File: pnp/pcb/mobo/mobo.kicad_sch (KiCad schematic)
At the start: 0 parts

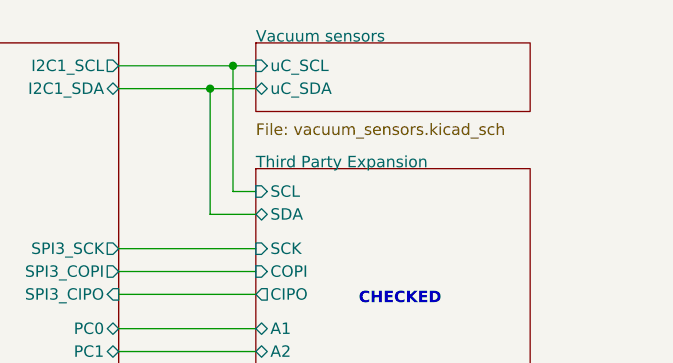
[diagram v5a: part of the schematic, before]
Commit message: Updated symbols and changed I2C multiplexer to a simpler one
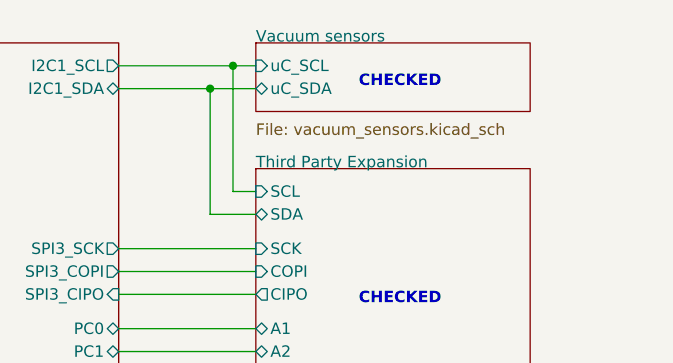
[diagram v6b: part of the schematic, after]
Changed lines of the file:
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@@
+    (effects (font (size 1.27 1.27) (thickness 0.254) bold (color 0 127 0 1)) (justify left bottom))
+  )
+  (text "CHECKED" (at 198.12 34.29 0)
     (effects (font (size 1.27 1.27) (thickness 0.254) bold (color 0 127 0 1)) (justify left bottom))
   )

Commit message: All pages checked
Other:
- note removed: "CHECKED"
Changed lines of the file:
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@@
     (stroke (width 0) (type default))
-  )
-  (text "CHECKED" (at 93.98 34.29 0)
-    (effects (font (size 1.27 1.27) (thickness 0.254) bold (color 0 127 0 1)) (justify left bottom))
   )
   (text "24V input\n5V generation\n3V3 generation" (at 132.08 177.8 0)
@@
     (effects (font (size 1.27 1.27)) (justify left bottom))
   )
-  (text "CHECKED" (at 97.79 135.89 0)
-    (effects (font (size 1.27 1.27) (thickness 0.254) bold (color 0 127 0 1)) (justify left bottom))
-  )
-  (text "CHECKED" (at 198.12 34.29 0)
-    (effects (font (size 1.27 1.27) (thickness 0.254) bold (color 0 127 0 1)) (justify left bottom))
-  )
-  (text "CHECKED" (at 90.17 81.28 0)
-    (effects (font (size 1.27 1.27) (thickness 0.254) bold (color 0 127 0 1)) (justify left bottom))
-  )
-  (text "CHECKED" (at 198.12 58.42 0)
-    (effects (font (size 1.27 1.27) (thickness 0.254) bold (color 0 127 0 1)) (justify left bottom))
-  )
   (sheet (at 85.09 43.18) (size 30.48 80.01)

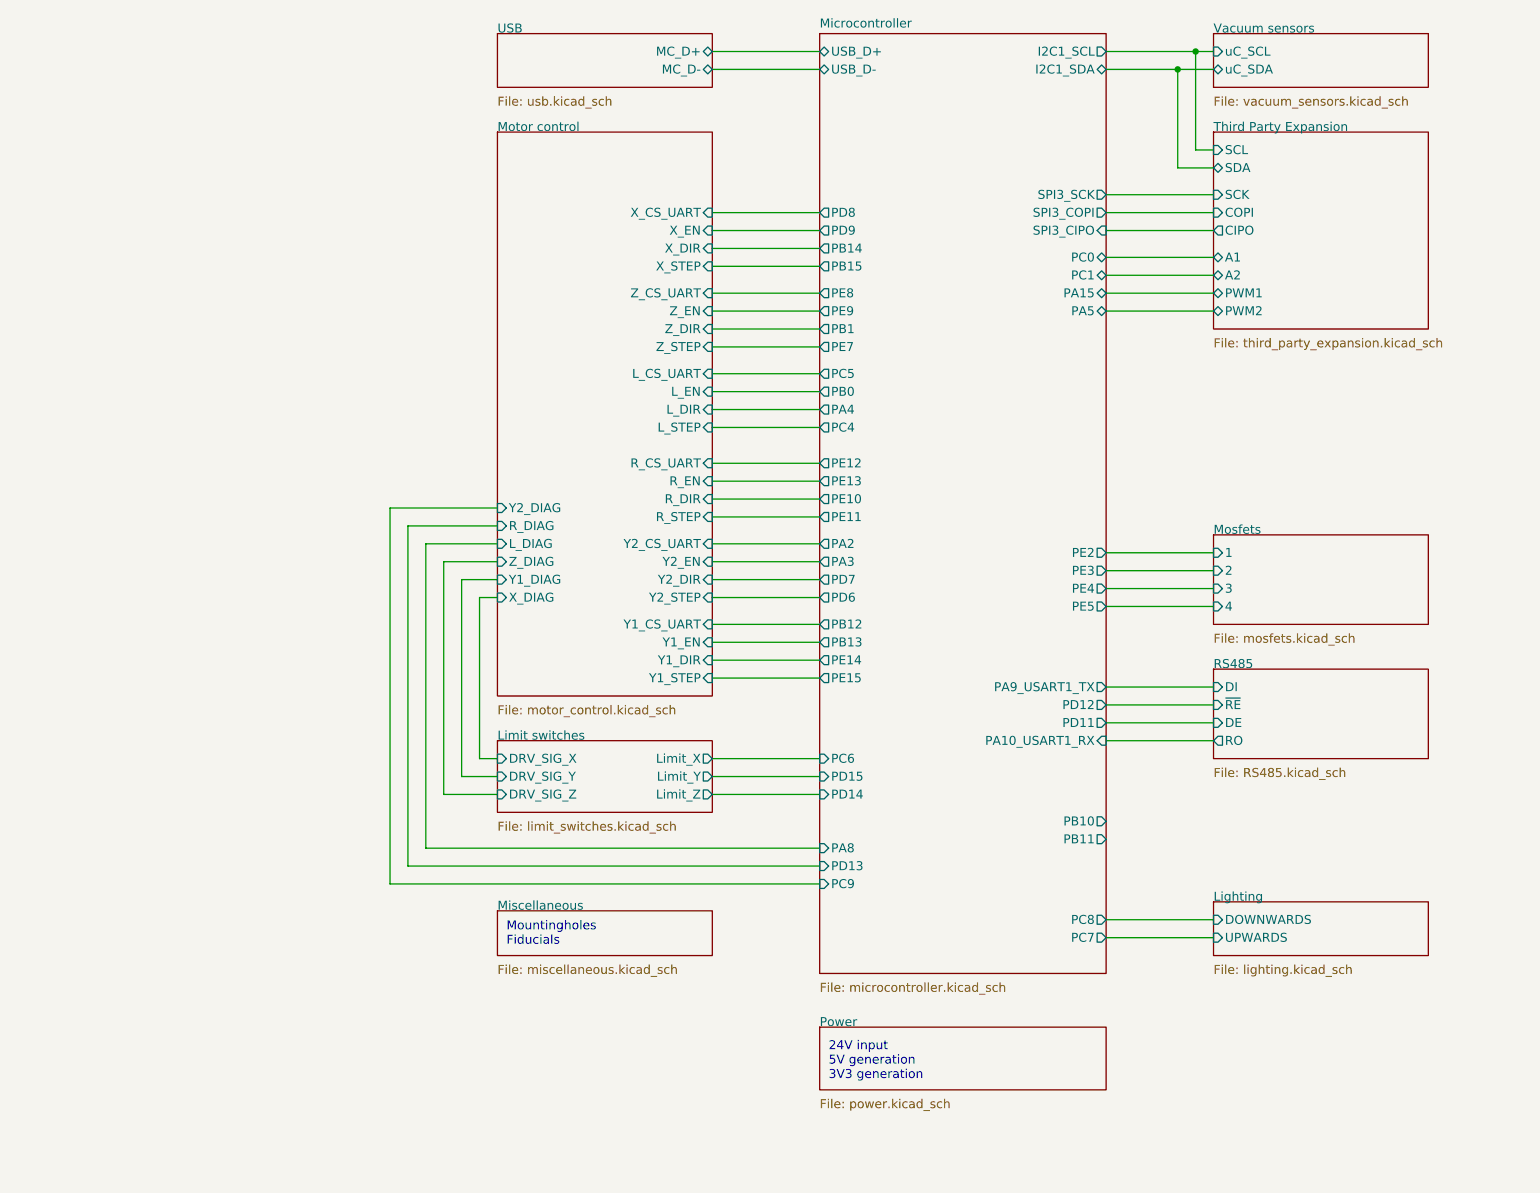
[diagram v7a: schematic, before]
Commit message: Schematic almost finished
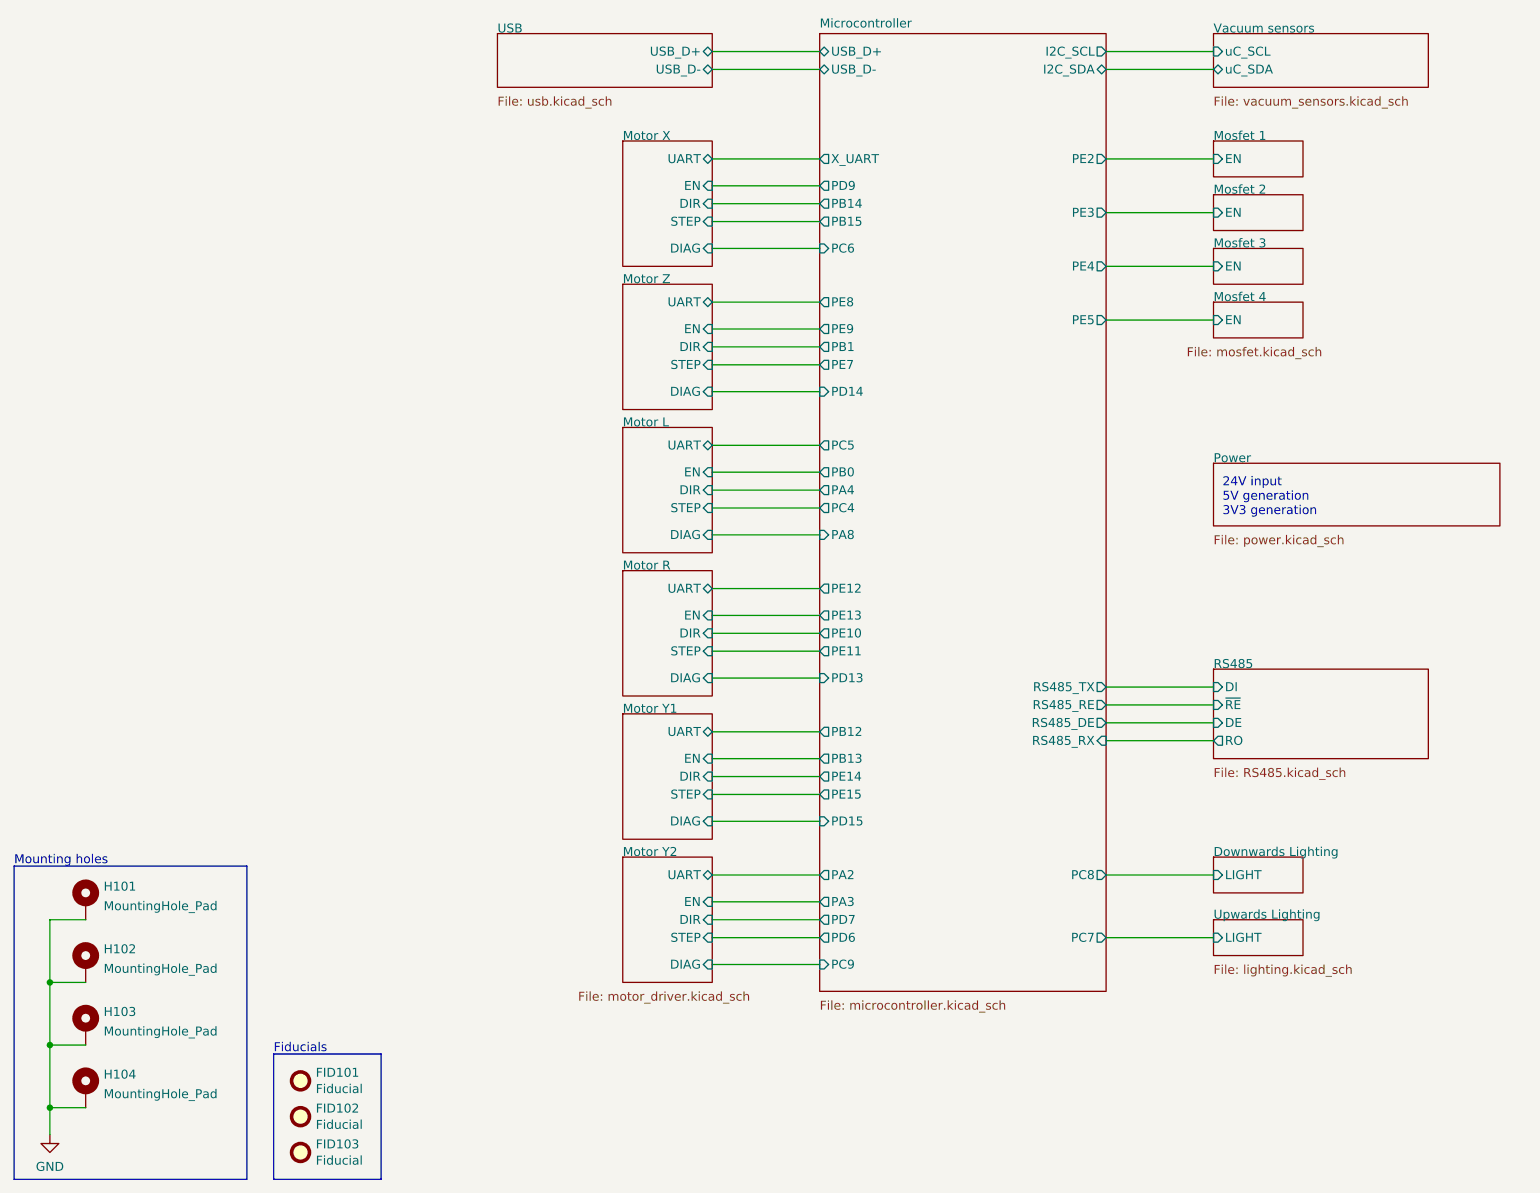
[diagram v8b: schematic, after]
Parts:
- added FID101, FID102, FID103: Fiducial, Fiducial:Fiducial_1mm_Mask2mm, symbol Mechanical:Fiducial
- added H101, H102, H103, H104: MountingHole_Pad, MountingHole:MountingHole_3.2mm_M3_DIN965_Pad, symbol Mechanical:MountingHole_Pad
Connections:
- new net GND: H101.1, H102.1, H103.1, H104.1
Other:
- sheet Lighting renamed Upwards Lighting
- removed sheet Limit switches
- removed sheet Miscellaneous
- removed sheet Mosfets
- removed sheet Motor control
- removed sheet Third Party Expansion
- added sheet Downwards Lighting (lighting.kicad_sch)
- added sheet Mosfet 1 (mosfet.kicad_sch)
- added sheet Mosfet 2 (mosfet.kicad_sch)
- added sheet Mosfet 3 (mosfet.kicad_sch)
- added sheet Mosfet 4 (mosfet.kicad_sch)
- added sheet Motor L (motor_driver.kicad_sch)
- added sheet Motor R (motor_driver.kicad_sch)
- added sheet Motor X (motor_driver.kicad_sch)
- added sheet Motor Y1 (motor_driver.kicad_sch)
- added sheet Motor Y2 (motor_driver.kicad_sch)
- added sheet Motor Z (motor_driver.kicad_sch)
- sheet Microcontroller ports: added I2C_SCL, I2C_SDA, RS485_DE, RS485_RE, RS485_RX, RS485_TX, X_UART; removed I2C1_SCL, I2C1_SDA, PA10_USART1_RX, PA15, PA5, PA9_USART1_TX, PB10, PB11, PC0, PC1, PD11, PD12, PD8, SPI3_CIPO, SPI3_COPI, SPI3_SCK
- sheet USB ports: added USB_D+, USB_D-; removed MC_D+, MC_D-
- sheet Upwards Lighting ports: added LIGHT; removed DOWNWARDS, UPWARDS
- note added: "Fiducials"
- note added: "Mounting holes"
- note removed: "Mountingholes Fiducials"
